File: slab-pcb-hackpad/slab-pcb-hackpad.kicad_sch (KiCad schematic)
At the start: 106 parts, among them J1 MagnetR, J2 MagnetL, J3 TRRS_R, J4 TRRS_L, J5 SSD1306, J6 Conn_01x06, Q1 MMBT3906, U1 Seeeduino Xiao rp2040, U2 PCA9555PW, U3 PCA9555PW, U4 SN74AHCT125PWR

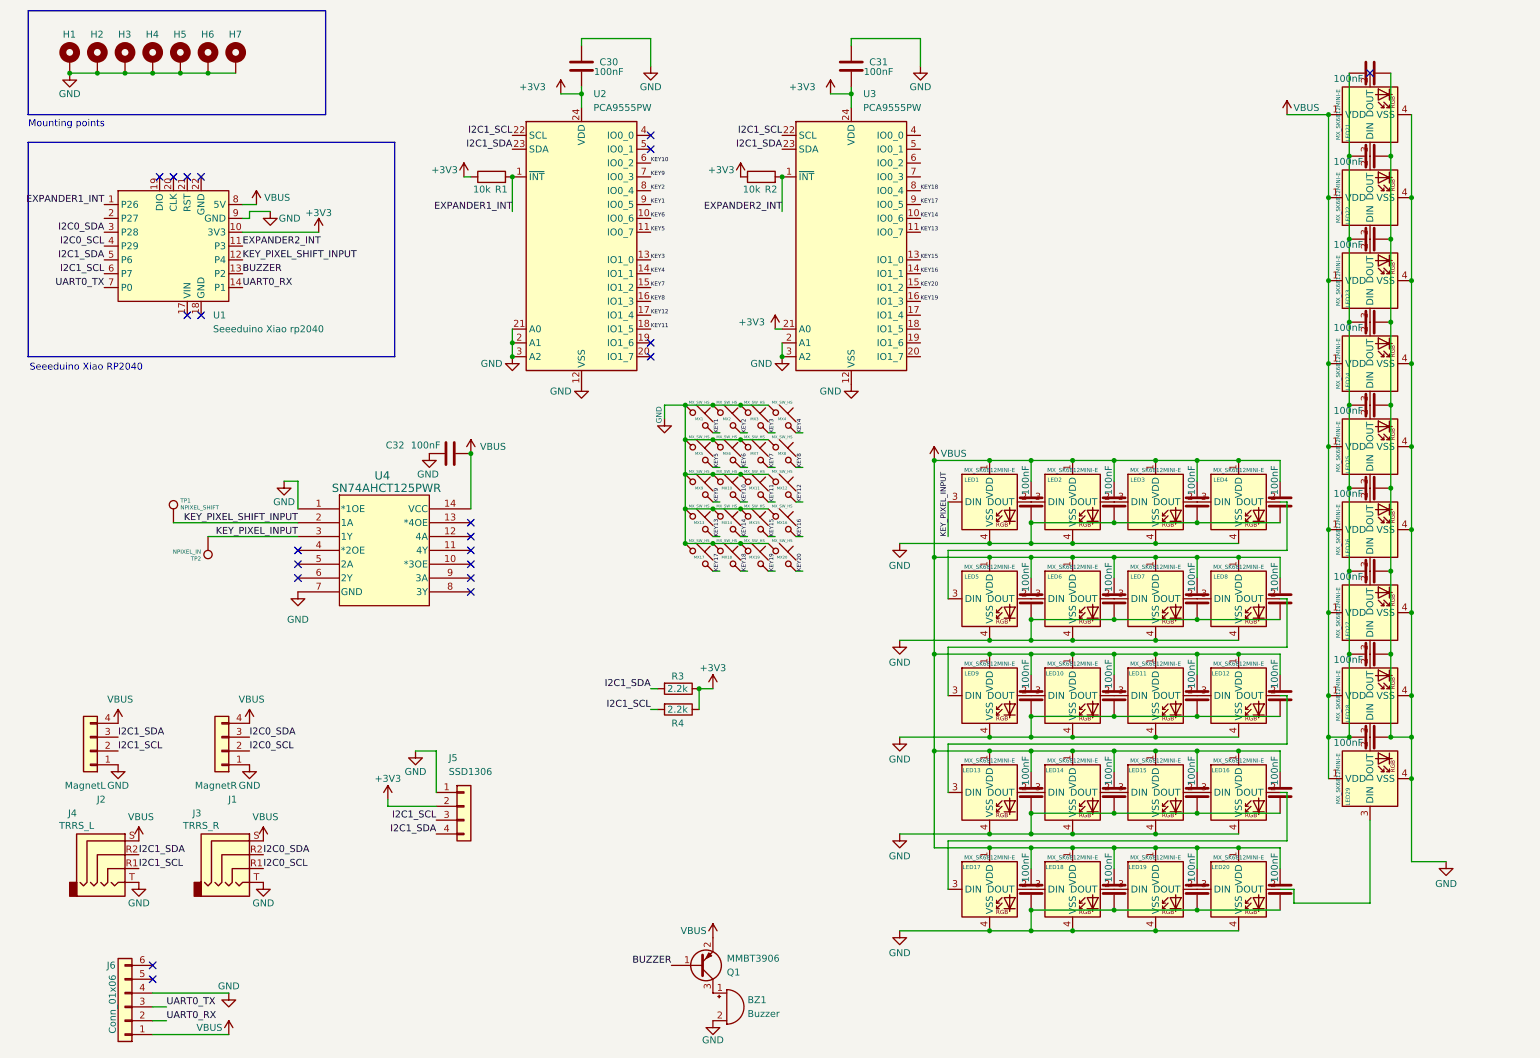
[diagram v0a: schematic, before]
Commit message: fix: inconsistent design
all modules now share the same design - with updated footprints to
support both choc+mx PCB mounting holes.
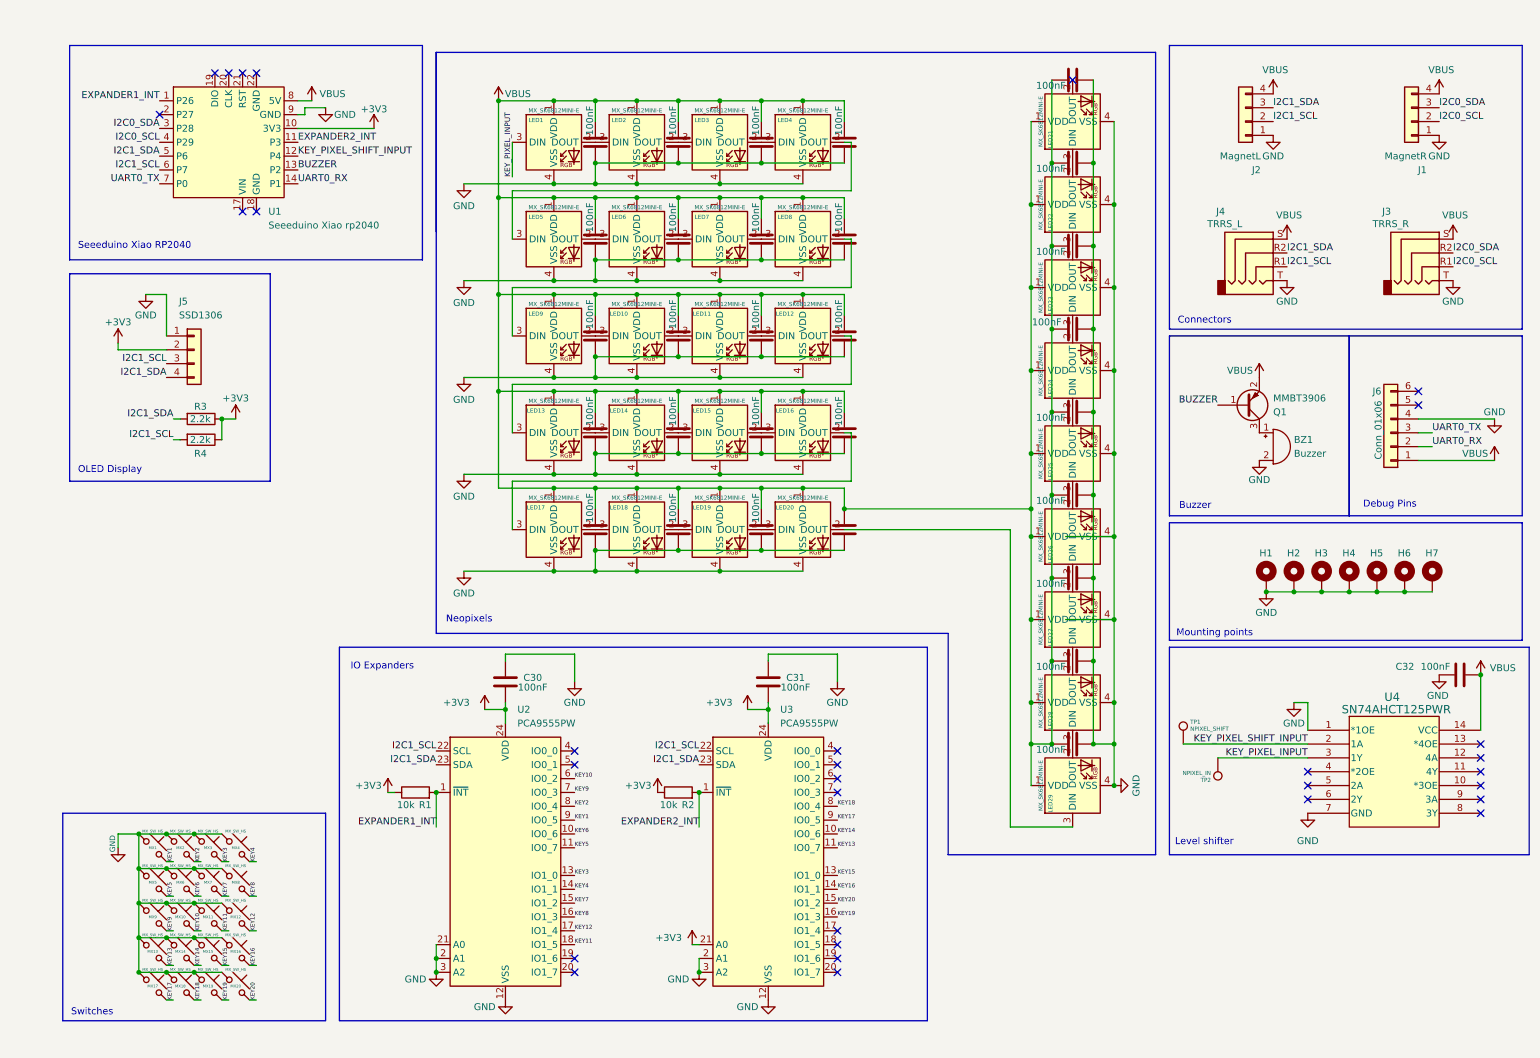
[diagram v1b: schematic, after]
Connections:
- no-connect marks 22 -> 31
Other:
- note added: "Buzzer"
- note added: "Connectors"
- note added: "Debug Pins"
- note added: "IO Expanders"
- note added: "Level shifter"
- note added: "Neopixels"
- note added: "OLED Display"
- note added: "Switches"
- company: (none) -> Edward Hesketh
- title: (none) -> Slab Keyboard - Hackpad Module
- moved on the sheet: C30, C31, C32, LED25, LED26, LED27, LED28, LED29, MX1, MX10, MX11, MX12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

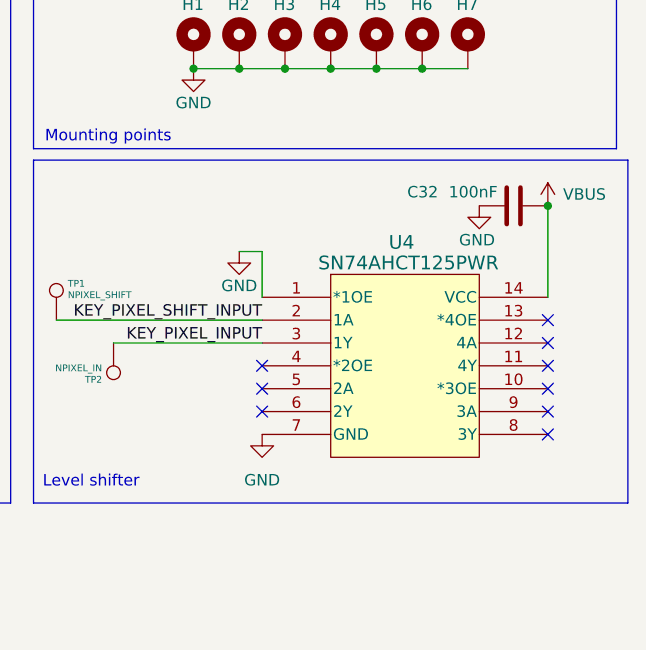
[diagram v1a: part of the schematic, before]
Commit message: chore: move shared files to a central directory
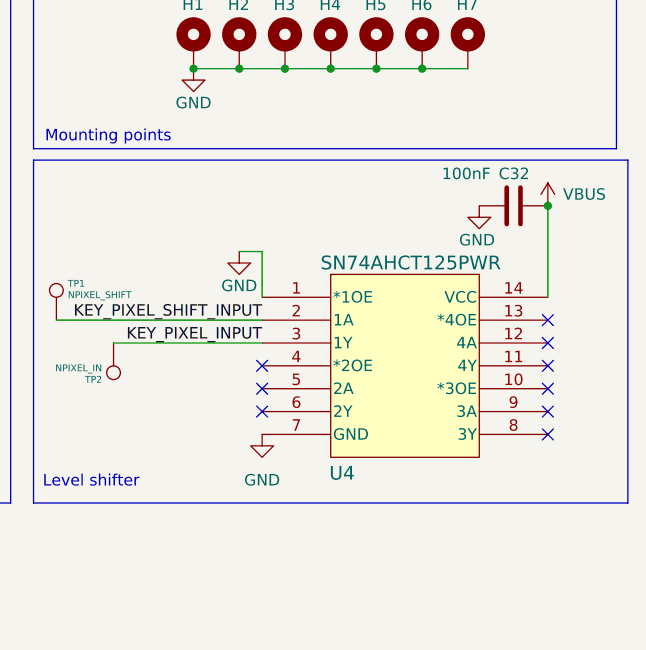
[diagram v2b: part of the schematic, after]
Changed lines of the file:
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@@
 	(symbol
 		(lib_id "CustomSymbols:SN74AHCT125PWR")
-		(at 242.57 140.97 0)
+		(at 259.08 147.32 0)
 		(unit 1)
 		(exclude_from_sim no)
@@
 		(dnp no)
 		(property "Reference" "U4"
-			(at 258.064 134.874 0)
+			(at 251.46 160.528 0)
 			(effects
 				(font
@@
 		)
 		(property "Value" "SN74AHCT125PWR"
-			(at 258.826 137.16 0)
+			(at 259.08 137.16 0)
 			(effects
 				(font
@@
 		)
 		(property "Footprint" "CustomFootprints:SN74AHCT125PWR"
-			(at 242.57 140.97 0)
+			(at 259.08 147.32 0)
 			(effects
 				(font
@@
 		)
 		(property "Datasheet" "SN74AHCT125PWR"
-			(at 242.57 140.97 0)
+			(at 251.46 149.86 0)
 			(effects
 				(font
@@
 		)
 		(property "Description" ""
-			(at 242.57 140.97 0)
+			(at 251.46 149.86 0)
 			(effects
 				(font
@@
 		(dnp no)
 		(property "Reference" "C32"
-			(at 262.128 129.286 90)
+			(at 272.288 127.254 90)
 			(effects
 				(font
@@
 		)
 		(property "Value" "100nF"
-			(at 268.732 129.286 90)
+			(at 267.97 127.254 90)
 			(effects
 				(font

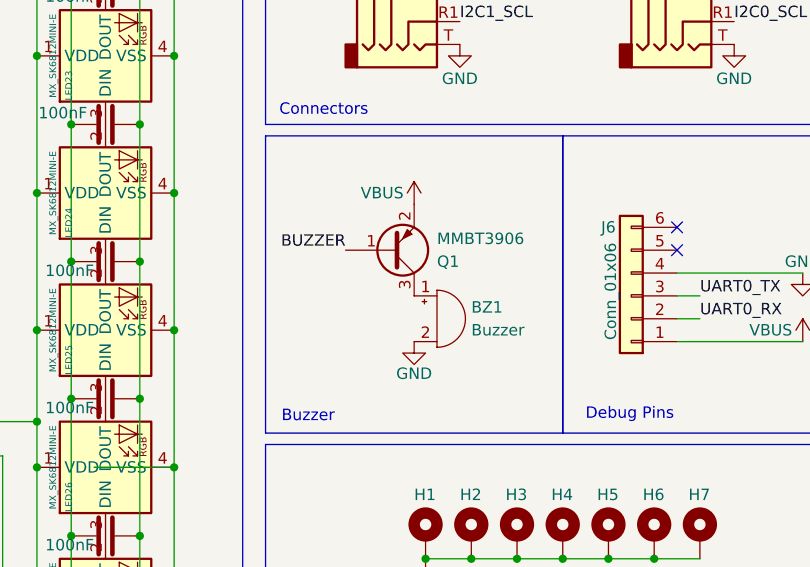
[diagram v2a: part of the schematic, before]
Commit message: feat: use slots instead of overlapped drill hits
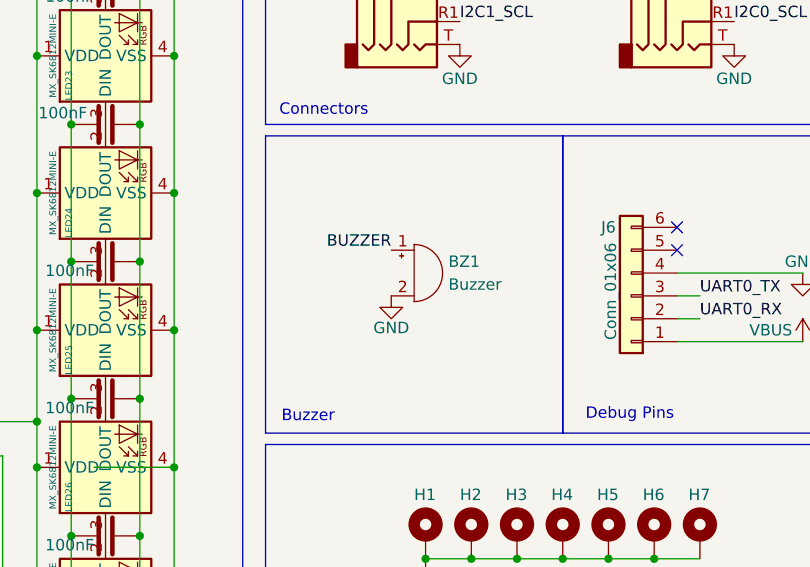
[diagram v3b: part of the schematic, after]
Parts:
- removed Q1: MMBT3906, Package_TO_SOT_SMD:SOT-23, symbol Transistor_BJT:MMBT3906
- BZ1: footprint Buzzer_Beeper:MagneticBuzzer_CUI_CMT-8504-100-SMT -> CustomFootprints:buzzer
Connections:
- net BUZZER: now also BZ1.1 (+)
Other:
- moved on the sheet: BZ1
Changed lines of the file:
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@@
 	)
 	(label "BUZZER"
-		(at 226.06 81.28 180)
+		(at 231.14 81.28 180)
 		(fields_autoplaced yes)
 		(effects
@@
 	(symbol
 		(lib_id "power:GND")
-		(at 233.68 91.44 0)
+		(at 231.14 86.36 0)
 		(unit 1)
 		(exclude_from_sim no)
@@
 		(dnp no)
 		(property "Reference" "#PWR036"
-			(at 233.68 97.79 0)
+			(at 231.14 92.71 0)
 			(effects
 				(font
@@
 		)
 		(property "Value" "GND"
-			(at 233.68 94.996 0)
+			(at 231.14 89.916 0)
 			(effects
 				(font
@@
 		)
 		(property "Footprint" ""
-			(at 233.68 91.44 0)
+			(at 231.14 86.36 0)
 			(effects
 				(font
@@
 		)
 		(property "Datasheet" ""
-			(at 233.68 91.44 0)
+			(at 231.14 86.36 0)
 			(effects
 				(font
@@
 		)
 		(property "Description" ""
-			(at 233.68 91.44 0)
+			(at 231.14 86.36 0)
 			(effects
 				(font
@@
 	(symbol
 		(lib_id "Device:Buzzer")
-		(at 236.22 88.9 0)
+		(at 233.68 83.82 0)
 		(unit 1)
 		(exclude_from_sim no)
@@
 		(fields_autoplaced yes)
 		(property "Reference" "BZ1"
-			(at 240.03 87.6299 0)
+			(at 237.49 82.5499 0)
 			(effects
 				(font
@@
 		)
 		(property "Value" "Buzzer"
-			(at 240.03 90.1699 0)
+			(at 237.49 85.0899 0)
 			(effects
 				(font
@@
 			)
 		)
-		(property "Footprint" "Buzzer_Beeper:MagneticBuzzer_CUI_CMT-8504-100-SMT"
-			(at 235.585 86.36 90)
+		(property "Footprint" "CustomFootprints:buzzer"
+			(at 233.045 81.28 90)
 			(effects
 				(font
@@
 		)
 		(property "Datasheet" "~"
-			(at 235.585 86.36 90)
+			(at 233.045 81.28 90)
 			(effects
 				(font
@@
 		)
 		(property "Description" "Buzzer, polarized"
-			(at 236.22 88.9 0)
+			(at 233.68 83.82 0)
 			(effects
 				(font
@@
 	)
 	(symbol
-		(lib_id "power:VBUS")
-		(at 233.68 76.2 0)
-		(unit 1)
-		(exclude_from_sim no)
-		(in_bom yes)
-		(on_board yes)
-		(dnp no)
-		(property "Reference" "#PWR034"
-			(at 233.68 80.01 0)
-			(effects
-				(font
-					(size 1.27 1.27)
-				)
-				(hide yes)
-			)
-		)
-		(property "Value" "VBUS"
-			(at 230.124 74.93 0)
-			(effects
-				(font
-					(size 1.27 1.27)
-				)
-			)
-		)
-		(property "Footprint" ""
-			(at 233.68 76.2 0)
-			(effects
-				(font
-					(size 1.27 1.27)
-				)
-				(hide yes)
-			)
-		)
-		(property "Datasheet" ""
-			(at 233.68 76.2 0)
-			(effects
-				(font
-					(size 1.27 1.27)
-				)
-				(hide yes)
-			)
-		)
-		(property "Description" "Power symbol creates a global label with name \"VBUS\""
-			(at 233.68 76.2 0)
-			(effects
-				(font
-					(size 1.27 1.27)
-				)
-				(hide yes)
-			)
-		)
-		(pin "1"
-		)
-		(instances
-			(project "slab-pcb-hackpad"
-				(path "/11417e3d-014f-4124-bb0b-1e020203d0fa"
-					(reference "#PWR034")
-					(unit 1)
-				)
-			)
-		)
-	)
-	(symbol
 		(lib_id "Device:C")
 		(at 142.24 86.36 180)
@@
 					(unit 1)
 				)
-			)
-		)
-	)
-	(symbol
-		(lib_id "Transistor_BJT:MMBT3906")
-		(at 231.14 81.28 0)
-		(mirror x)
-		(unit 1)
-		(exclude_from_sim no)
-		(in_bom yes)
-		(on_board yes)
-		(dnp no)
-		(property "Reference" "Q1"
-			(at 236.22 82.5501 0)
-			(effects
-				(font
-					(size 1.27 1.27)
-				)
-				(justify left)
-			)
-		)
-		(property "Value" "MMBT3906"
-			(at 236.22 80.0101 0)
-			(effects
-				(font
-					(size 1.27 1.27)
-				)
-				(justify left)
-			)
-		)
-		(property "Footprint" "Package_TO_SOT_SMD:SOT-23"
-			(at 236.22 79.375 0)
-			(effects
-				(font
-					(size 1.27 1.27)
-					(italic yes)
-				)
-				(justify left)
-				(hide yes)
-			)
-		)
-		(property "Datasheet" "https://www.onsemi.com/pdf/datasheet/pzt3906-d.pdf"
-			(at 231.14 81.28 0)
-			(effects
-				(font
-					(size 1.27 1.27)
-				)
-				(justify left)
-				(hide yes)
-			)
-		)
-		(property "Description" "-0.2A Ic, -40V Vce, Small Signal PNP Transistor, SOT-23"
-			(at 231.14 81.28 0)
-			(effects
-				(font
-					(size 1.27 1.27)
-				)
-				(hide yes)
-			)
-		)
-		(pin "1"
-		)
-		(pin "3"
-		)
-		(pin "2"
-		)
-		(instances
-			(project "slab-pcb-hackpad"
-				(path "/11417e3d-014f-4124-bb0b-1e020203d0fa"
-					(reference "Q1")
-					(unit 1)
-				)
